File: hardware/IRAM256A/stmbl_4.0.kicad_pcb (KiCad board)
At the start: 2 copper layers, 100 x 100 mm, 433 parts, among them J1 RJ45_LED, J2 RJ45_LED, J3 RJ45_LED, P1 USB_OTG, P10 CONN_02X06, P11 USB_OTG, P12 CONN_01X04, P13 CONN_01X04, P14 CONN_01X04, P15 CONN_01X02, P2 CONN_01X02, P3 CONN_01X02, P4 CONN_01X02, P5 CONN_01X06, P6 CONN_01X02, P7 CONN_01X04, P8 CONN_01X03, P9 CONN_01X06, Q1 IRLML6344, Q2 IRLML6344, Q3 IRLML6344, Q4 IRLML6344, Q5 IRLML6344, T1 testpoint, T2 testpoint, T44 testpoint, T45 testpoint, T46 testpoint, U1 USBLC6-4SC6, U10 SN65176B, U11 SN65176B, U12 IRAM256a, U13 ACT4088, U14 SN65176B, U15 SN65176B, U16 SN65176B, U17 SN65176B, U18 SN65176B, U19 SN65176B, U2 zldo1117, U20 USBLC6-4SC6, U21 USBLC6-4SC6, U22 USBLC6-4SC6, U23 USBLC6-4SC6, U24 non_plated, U25 STM32F303CBTx, U26 STM32F405VG, U27 ACT4088, U28 ACT4088, U29 USBLC6-4SC6, U3 SI8621, U30 non_plated, U31 non_plated, U32 non_plated, U33 heatsink, U34 fan, U35 non_plated, U36 non_plated, U37 non_plated, U39 non_plated, U4 ACT4088, U5 LNK304D, U6 LM358, U7 LM358, U8 SN65176B, U9 SN65176B, Y1 8M, Y2 8M

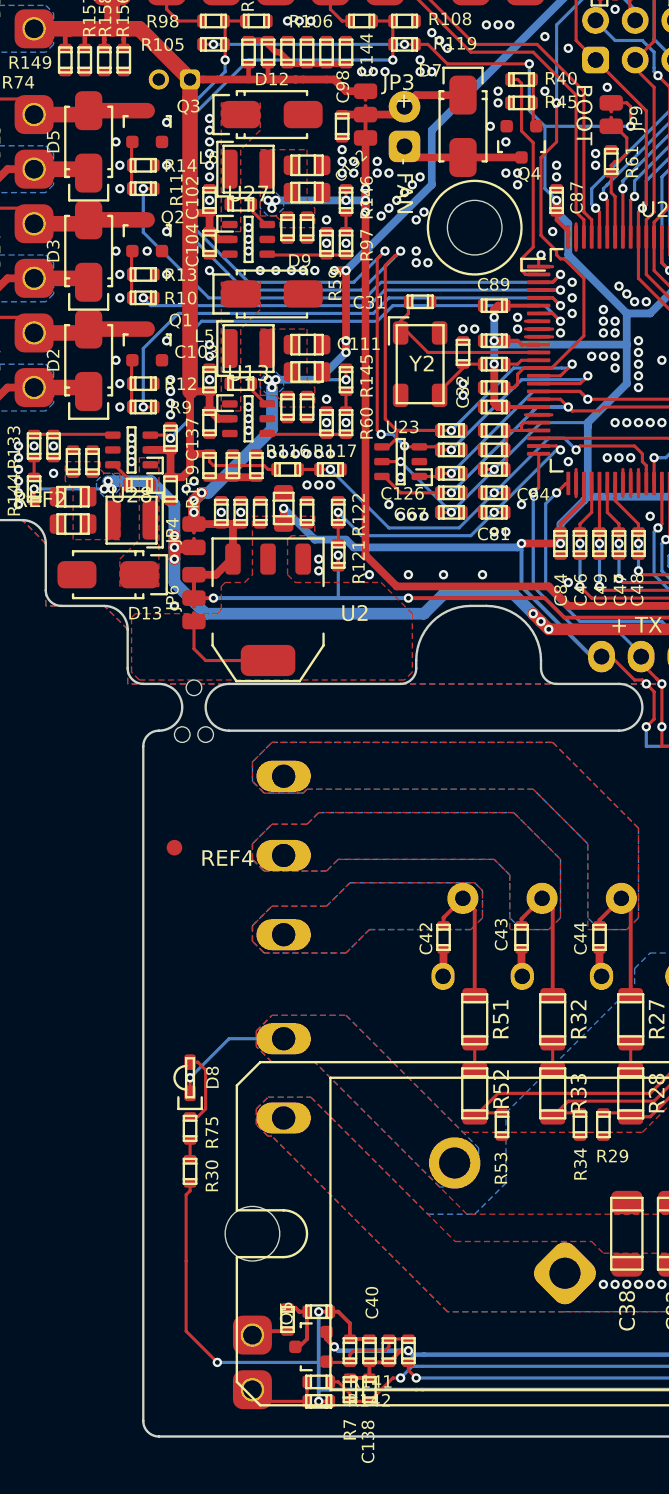
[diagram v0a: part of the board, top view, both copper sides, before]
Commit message: Structure change + kicad 3d models updated
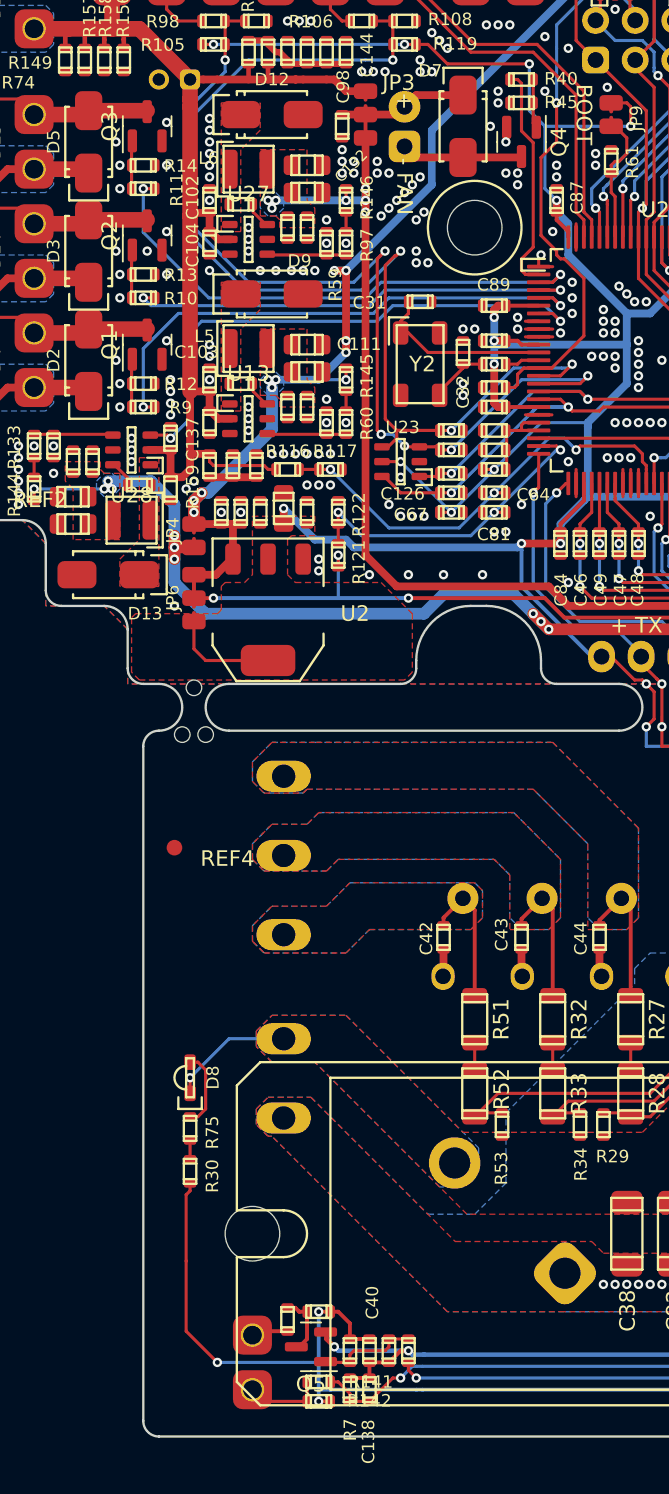
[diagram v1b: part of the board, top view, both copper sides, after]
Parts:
- Q1, Q2, Q3, Q4, Q5: footprint stmbl:SOT-23 -> Package_TO_SOT_SMD:SOT-23
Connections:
- net /ctrl/f4/CMD_12 renamed /ctrl/CMD/D12
- net /ctrl/f4/CMD_12E renamed /ctrl/CMD/E12
- net /ctrl/f4/CMD_36 renamed /ctrl/CMD/D36
- net /ctrl/f4/CMD_36E renamed /ctrl/CMD/E36
- net /ctrl/f4/CMD_45 renamed /ctrl/CMD/D45
- net /ctrl/f4/CMD_45E renamed /ctrl/CMD/E45
- net /ctrl/f4/CMD_78 renamed /ctrl/CMD/D78
- net /ctrl/f4/CMD_78E renamed /ctrl/CMD/E78
- net /ctrl/f4/CMD_L1 renamed /ctrl/CMD/L1
- net /ctrl/f4/CMD_L2 renamed /ctrl/CMD/L2
- net /ctrl/f4/FB0_L1 renamed /ctrl/FB0/L1
- net /ctrl/f4/FB0_L2 renamed /ctrl/FB0/L2
- net /ctrl/f4/FB1_L1 renamed /ctrl/FB1/L1
- net /ctrl/f4/FB1_L2 renamed /ctrl/FB1/L2
- net /ctrl/f4/IO_AIN0 renamed /ctrl/IO/IO_IN0
- net /ctrl/f4/IO_AIN1 renamed /ctrl/IO/IO_IN1
- net /hv/driver/CUH renamed /hv/cur/IU
- net /hv/driver/CVH renamed /hv/cur/IV
- net /hv/driver/CWH renamed /hv/cur/IW
- net /hv/f3/A_HV renamed /hv/back-emf/HV_
- net /hv/f3/A_T_HV renamed /hv/driver/Vth
- net /hv/f3/A_U renamed /hv/back-emf/U_
- net /hv/f3/A_V renamed /hv/back-emf/V_
- net /hv/f3/A_W renamed /hv/back-emf/W_
- net /hv/f3/HV_EN renamed /hv/driver/en
- P1 pad 1: (no net) -> unconnected-(P1-Pad1)
- P1 pad 4: (no net) -> unconnected-(P1-Pad4)
- P11 pad 1: (no net) -> unconnected-(P11-Pad1)
- P11 pad 4: (no net) -> unconnected-(P11-Pad4)
- U1 pad 4: (no net) -> unconnected-(U1-Pad4)
- U1 pad 6: (no net) -> unconnected-(U1-Pad6)
- U13 pad 3: (no net) -> unconnected-(U13-Pad3)
- U21 pad 4: (no net) -> unconnected-(U21-Pad4)
- U27 pad 3: (no net) -> unconnected-(U27-Pad3)
- U4 pad 3: (no net) -> unconnected-(U4-Pad3)
